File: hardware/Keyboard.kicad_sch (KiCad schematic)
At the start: 23 parts, among them J1 USB_C_Receptacle_USB2.0_16P, SW1 SW_Push, SW2 SW_Push, U1 STM32F072CBTx, U2 XC6206PxxxMR

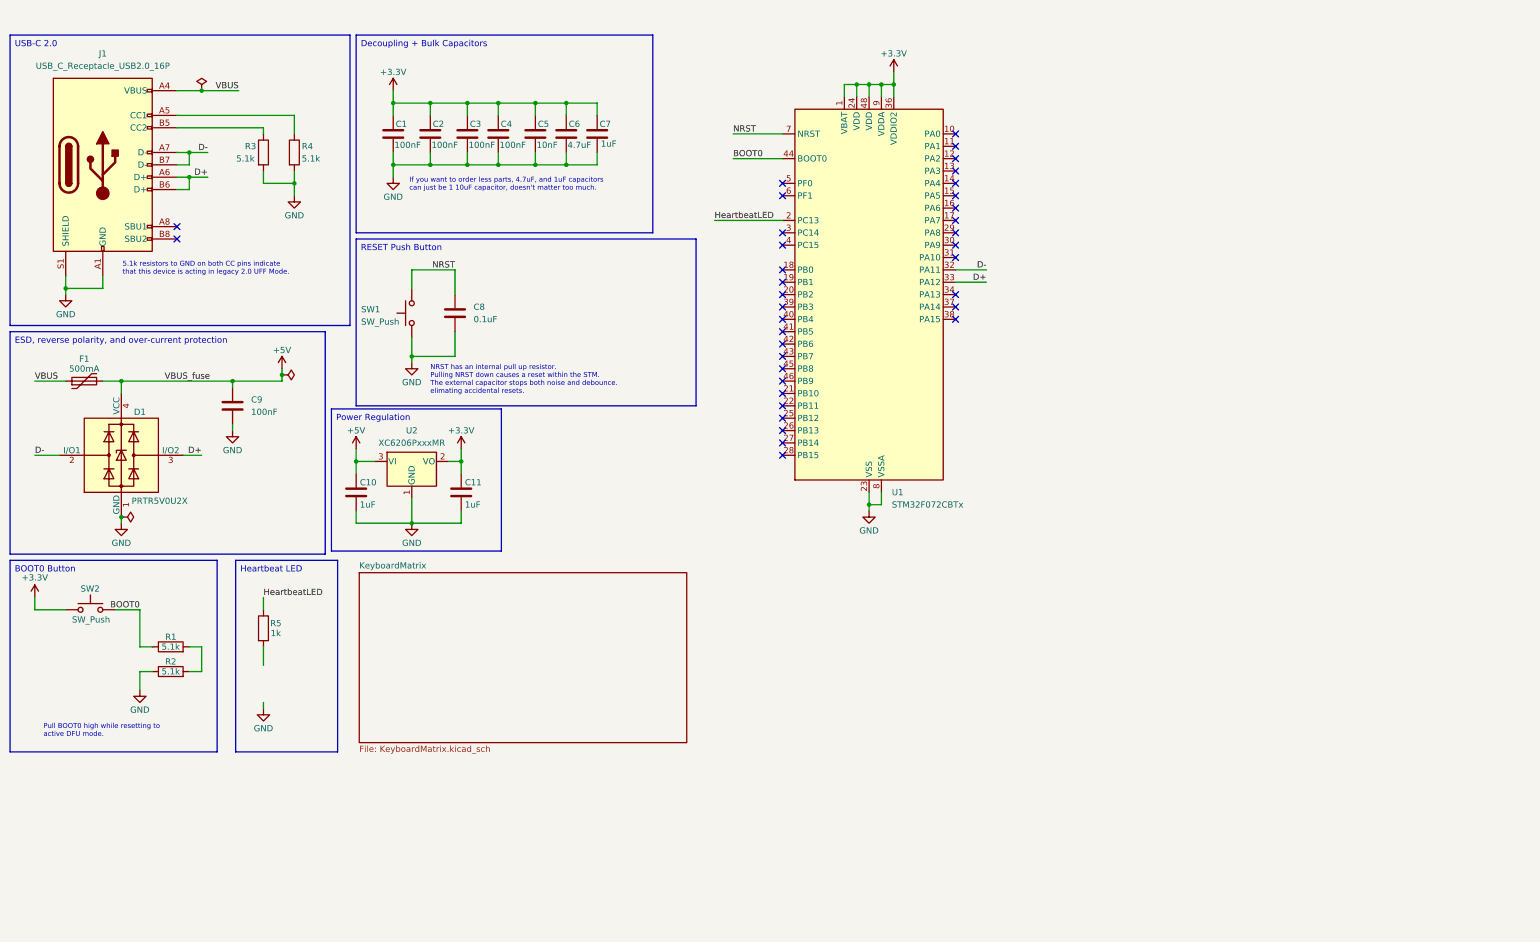
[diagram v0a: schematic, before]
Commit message: stm32layout done, started routing board
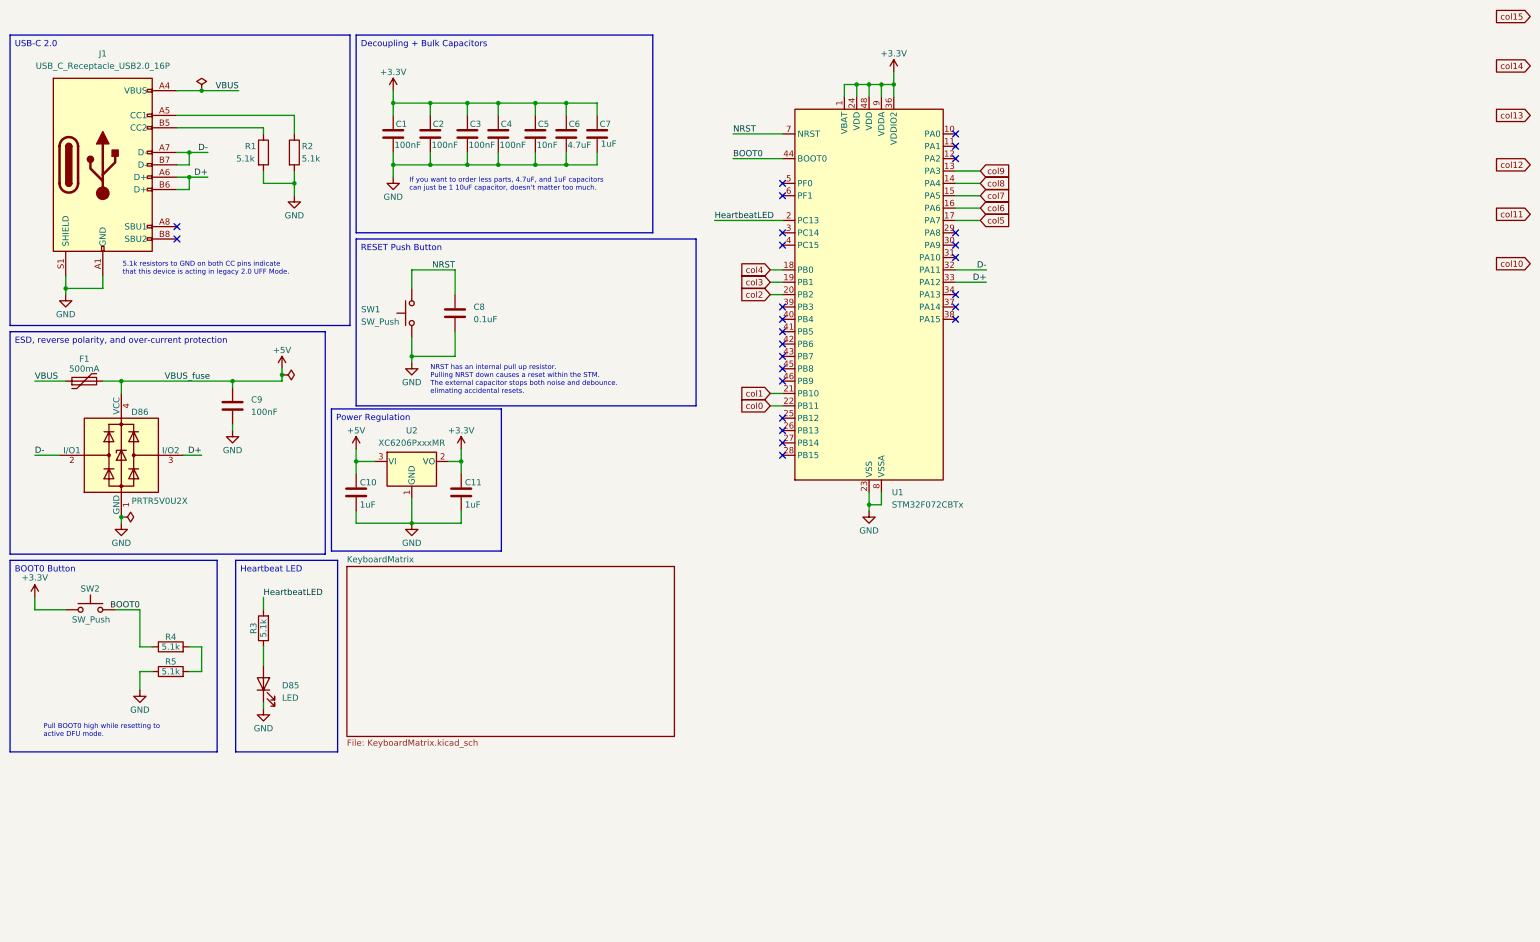
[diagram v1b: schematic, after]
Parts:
- removed R5: 1k, symbol Device:R
- added D85: LED, LED_SMD:LED_0603_1608Metric_Pad1.05x0.95mm_HandSolder, symbol Device:LED
- added R3: 5.1k, Resistor_SMD:R_0603_1608Metric_Pad0.98x0.95mm_HandSolder, symbol Device:R
- C1, C10, C11, C2, C3, C4, C5, C6, C7, C8, C9: footprint (none) -> Capacitor_SMD:C_0603_1608Metric_Pad1.08x0.95mm_HandSolder
- F1: footprint (none) -> Fuse:Fuse_0603_1608Metric
- J1: footprint (none) -> PCM_marbastlib-various:USB_C_Receptacle_HRO_TYPE-C-31-M-23
- R1: renamed from R3; footprint (none) -> Resistor_SMD:R_0603_1608Metric_Pad0.98x0.95mm_HandSolder
- R2: renamed from R4; footprint (none) -> Resistor_SMD:R_0603_1608Metric_Pad0.98x0.95mm_HandSolder
- R4: renamed from R1; footprint (none) -> Resistor_SMD:R_0603_1608Metric_Pad0.98x0.95mm_HandSolder
- R5: renamed from R2; footprint (none) -> Resistor_SMD:R_0603_1608Metric_Pad0.98x0.95mm_HandSolder
- SW1, SW2: footprint (none) -> Button_Switch_SMD:SW_Push_SPST_NO_Alps_SKRK
- renumbered D1 to D86
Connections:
- net GND: now also D85.1 (K)
- net HeartbeatLED: now also R3.2
- net col9: now reaches U1.13 (PA3)
- net col8: now reaches U1.14 (PA4)
- net col7: now reaches U1.15 (PA5)
- net col6: now reaches U1.16 (PA6)
- net col5: now reaches U1.17 (PA7)
- net col4: now reaches U1.18 (PB0)
- net col3: now reaches U1.19 (PB1)
- net col2: now reaches U1.20 (PB2)
- net col1: now reaches U1.21 (PB10)
- net col0: now reaches U1.22 (PB11)
- new net: D85.2 (A), R3.1
- no-connect marks 36 -> 26

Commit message: finished routing --> need to add test points and add i2c display. also need to request a review and refine routing.
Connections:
- net col10: now also U1.10 (PA0)
- net col11: now also U1.11 (PA1)
- net col12: now also U1.12 (PA2)
- net col13: now also U1.6 (PF1)
- net col14: now also U1.5 (PF0)
- net col15: now also U1.3 (PC14)
- net row0: now reaches U1.28 (PB15)
- net row5: now reaches U1.39 (PB3)
- net row4: now reaches U1.40 (PB4)
- net row3: now reaches U1.41 (PB5)
- net row2: now reaches U1.45 (PB8)
- net row1: now reaches U1.46 (PB9)
- no-connect marks 26 -> 14

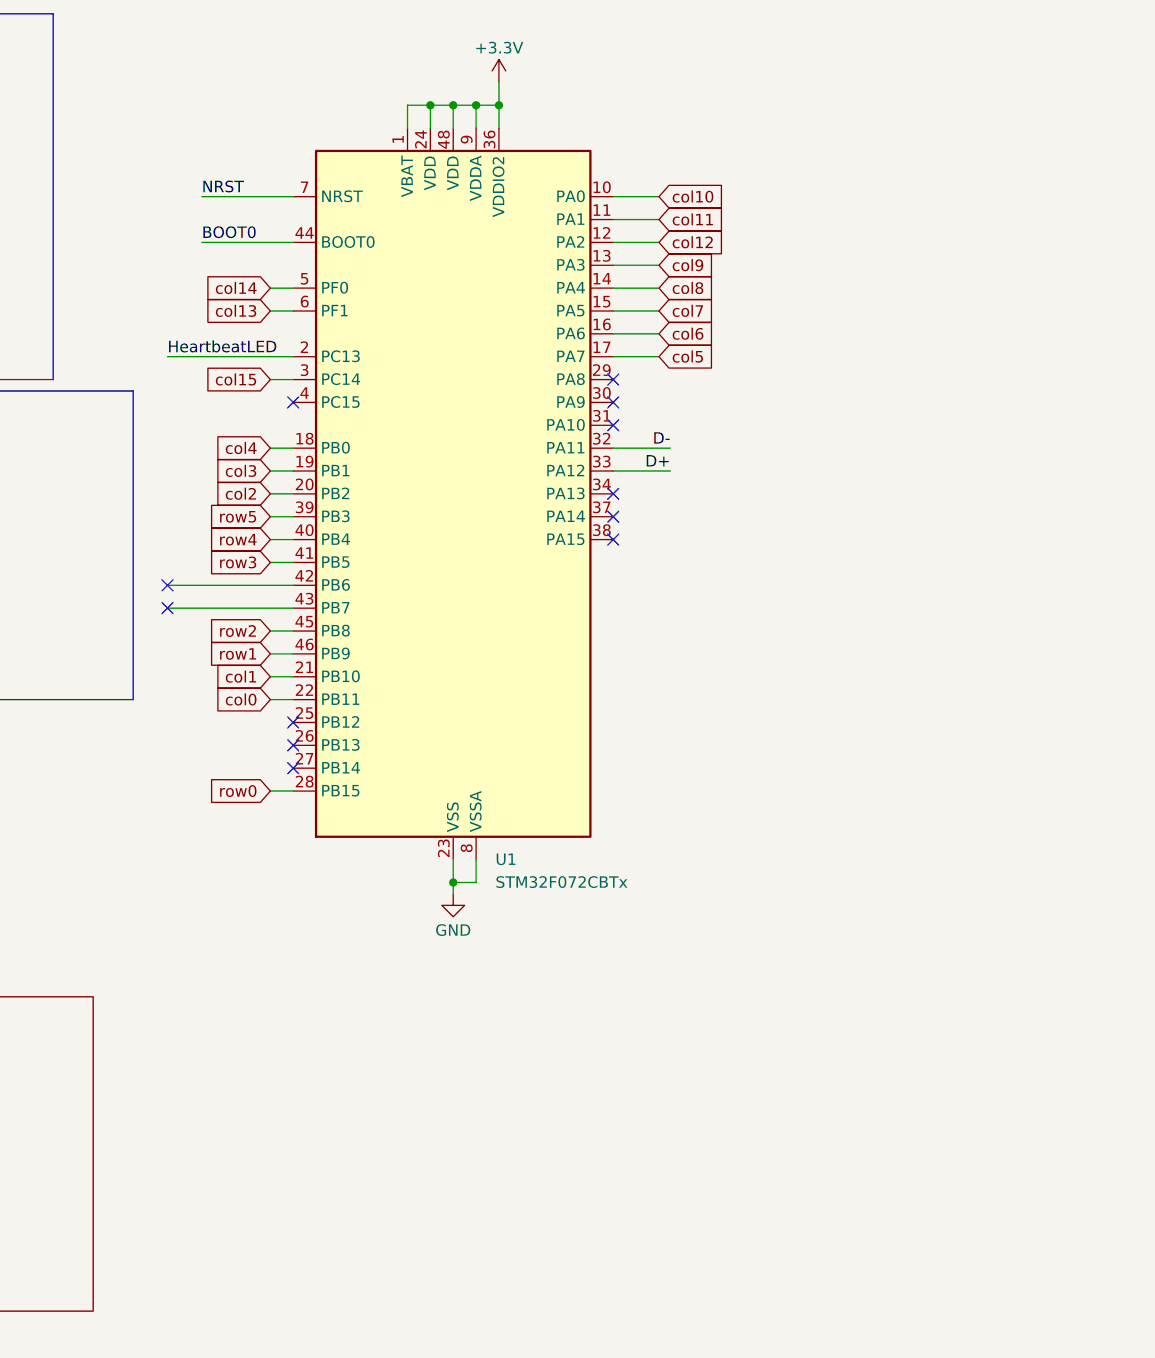
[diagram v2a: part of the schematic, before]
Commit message: added OLED display + new libary for it
things to add:
test points
3.3v, 5v LED
fix some wiring
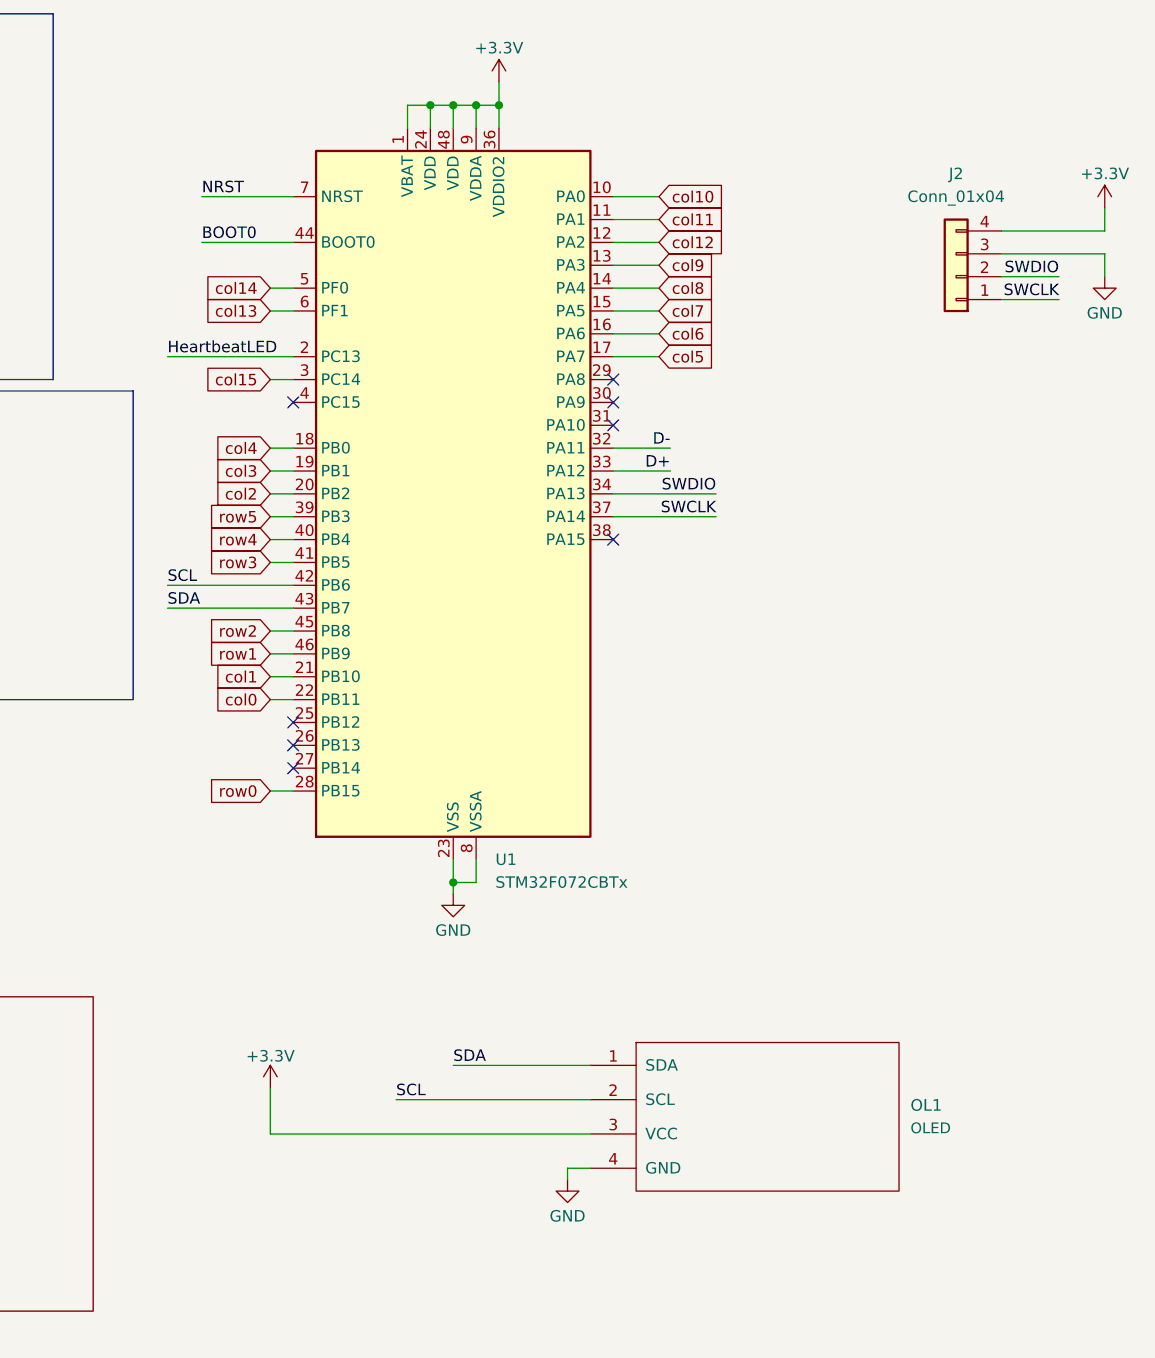
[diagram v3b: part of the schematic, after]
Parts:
- added J2: Conn_01x04, Connector_PinHeader_2.54mm:PinHeader_1x04_P2.54mm_Vertical, symbol Connector_Generic:Conn_01x04
- added OL1: OLED, kbd:OLED, symbol kbd:OLED
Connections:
- net +3.3V: now also J2.4 (Pin_4), OL1.3 (VCC)
- net GND: now also J2.3 (Pin_3), OL1.4 (GND)
- net SWDIO: now reaches U1.34 (PA13)
- net SWDIO: now also J2.2 (Pin_2)
- net SWCLK: now reaches U1.37 (PA14)
- net SWCLK: now also J2.1 (Pin_1)
- net SCL: now reaches U1.42 (PB6)
- net SCL: now also OL1.2 (SCL)
- net SDA: now reaches U1.43 (PB7)
- net SDA: now also OL1.1 (SDA)
- no-connect marks 14 -> 10

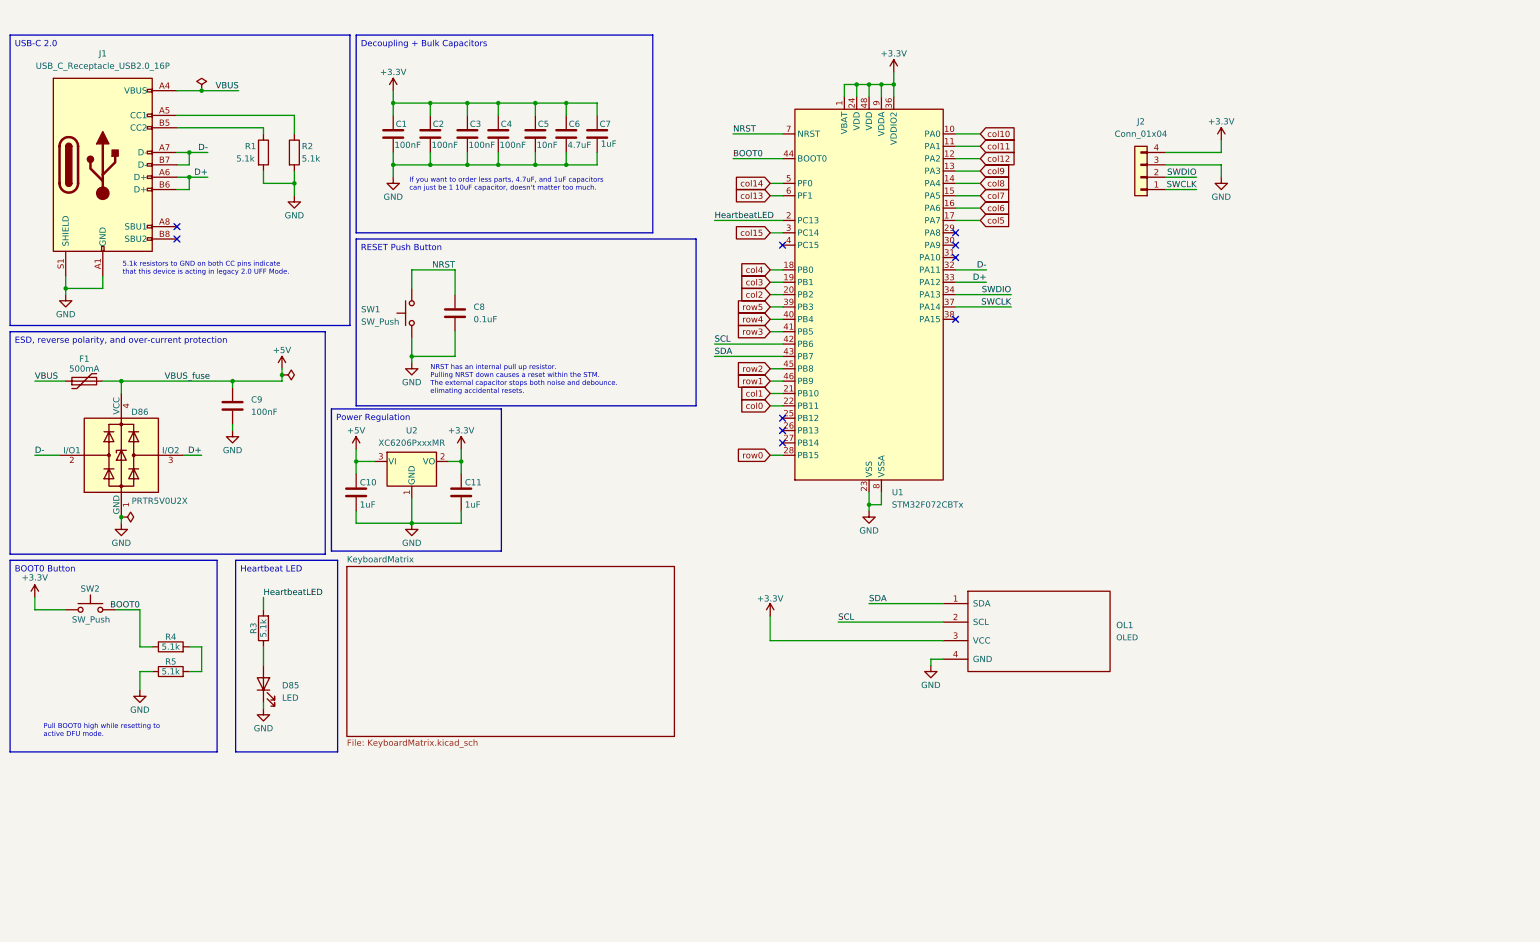
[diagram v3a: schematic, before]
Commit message: added testpoints, need to readd library
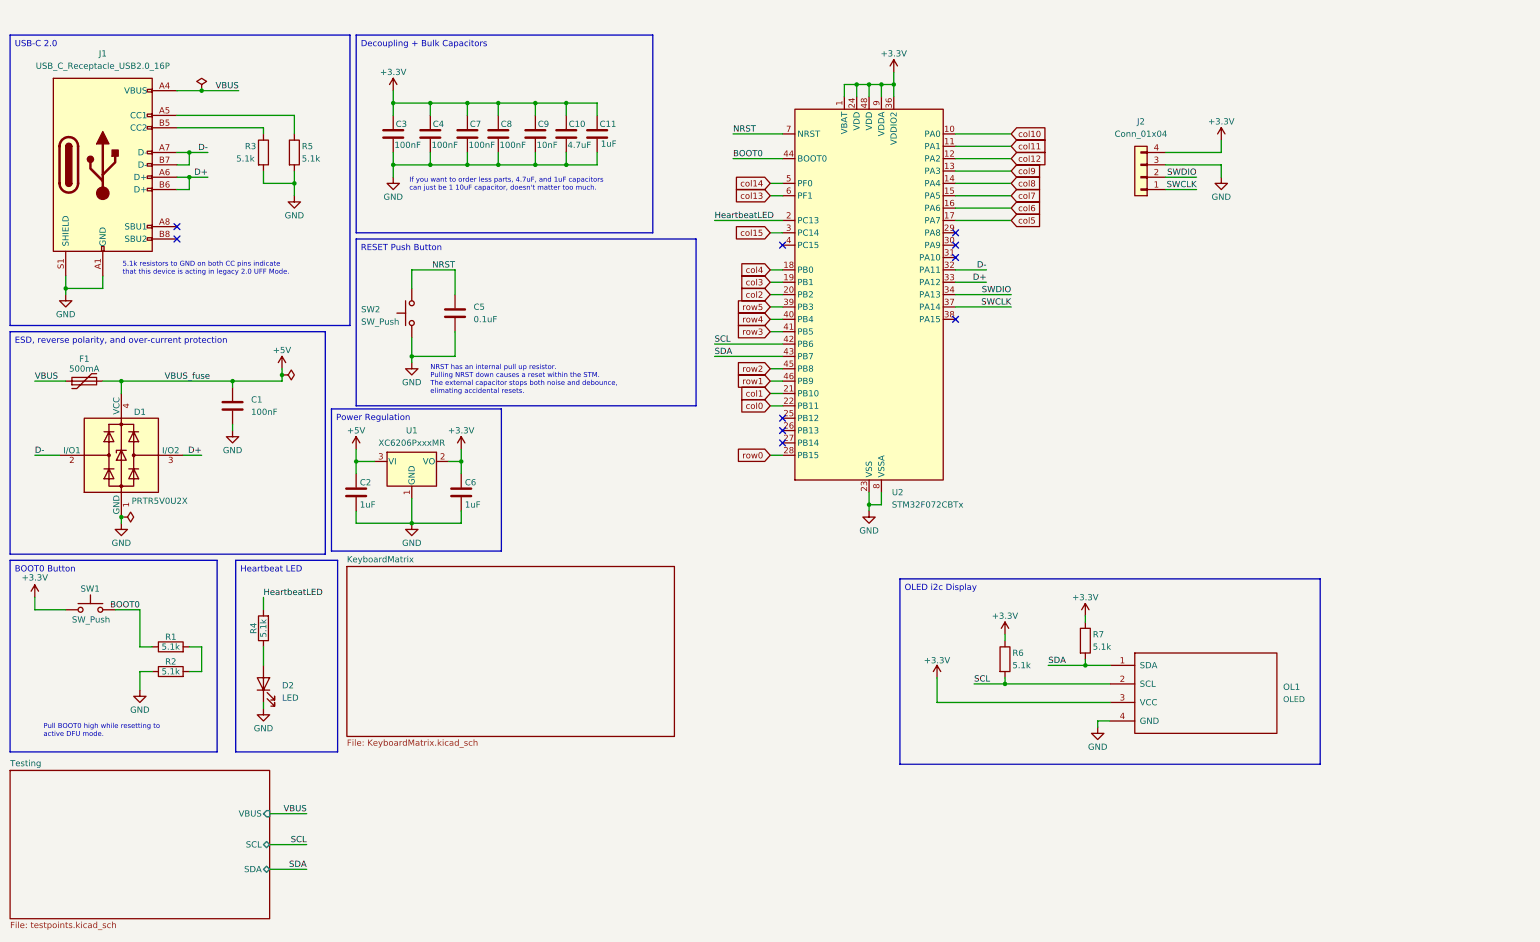
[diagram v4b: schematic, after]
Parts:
- added R6, R7: 5.1k, Resistor_SMD:R_0603_1608Metric_Pad0.98x0.95mm_HandSolder, symbol Device:R
- renumbered C9 to C1, C6 to C10, C7 to C11, C10 to C2, C1 to C3, C2 to C4, C8 to C5, C11 to C6, C3 to C7, C4 to C8, C5 to C9, D86 to D1, D85 to D2, R4 to R1, R5 to R2, R1 to R3, R3 to R4, R2 to R5, SW2 to SW1, SW1 to SW2, U2 to U1, U1 to U2
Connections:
- net +3.3V: now also R6.1, R7.1
- net SCL: now also R6.2
- net SDA: now also R7.2
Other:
- added sheet Testing (testpoints.kicad_sch)
- note added: "NRST has an internal pull up resistor. Pulling NRST down causes a reset within the STM. The external capacitor stops both noise and debounce, elimating accidental resets."
- note removed: "NRST has an internal pull up resistor. Pulling NRST down causes a reset within the STM. The external capacitor stops both noise and debounce. elimating accidental resets."
- moved on the sheet: OL1
